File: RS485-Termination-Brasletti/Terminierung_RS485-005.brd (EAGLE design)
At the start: 14 x 23 mm, 9 parts, among them IC1 REG1117, X1 1751264

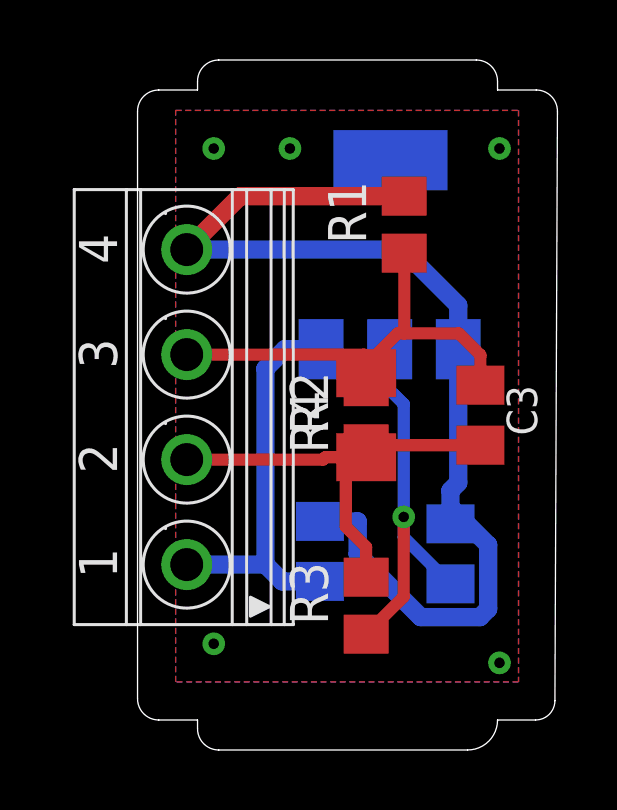
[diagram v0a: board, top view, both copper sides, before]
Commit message: Update RS485 Termin
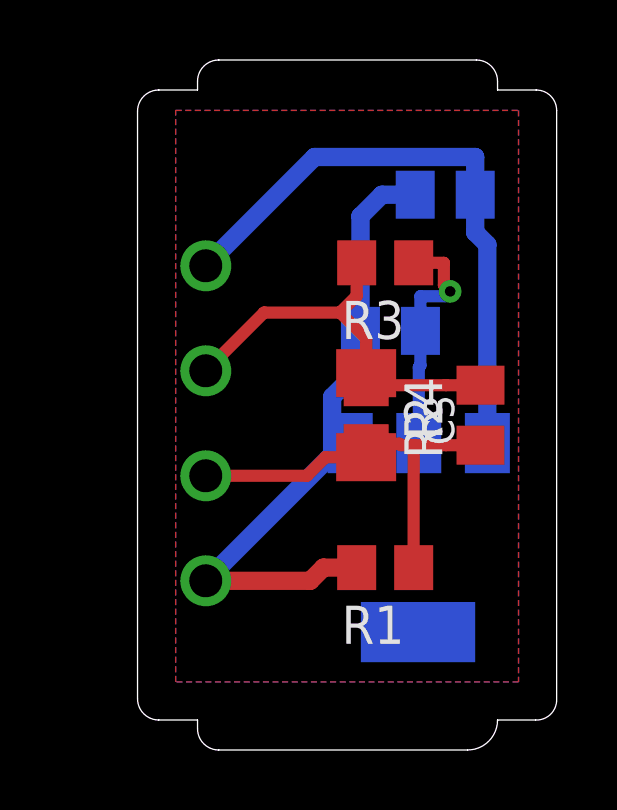
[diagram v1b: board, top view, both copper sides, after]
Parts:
- moved C1 12.6 mm to (10.3, 17.5), turned to 0 degrees
- moved R1 11.4 mm to (8.26, 5.08), turned to 180 degrees
- moved R3 11.4 mm to (8.26, 15.2), turned to 180 degrees
- moved IC1 9.47 mm to (9.35, 6.08), turned to 180 degrees
- moved C2 7.69 mm to (8.43, 13.0), turned to 0 degrees
- moved X1 0.83 mm to (2.17, 9.89), flipped to the bottom, turned to 270 degrees
- turned C3 to 90 degrees
- turned R2 to 270 degrees
- turned R4 to 270 degrees
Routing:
- net GND: track 36.8 -> 22.2 mm, vias 5 -> 0
- net VCC: track 13.3 -> 20.2 mm
- net N$2: track 13.1 -> 8.02 mm
- net N$3: track 15.2 -> 14.1 mm
- net N$4: track 14.6 -> 13.8 mm
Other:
- outline, holes or cut-outs redrawn
